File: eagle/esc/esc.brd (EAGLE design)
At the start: 101.6 x 50.8 mm, 88 parts, among them IC1 DRV8305NPHPR, IC2 STM32L431CCT6LQFP48, IC3 FT232RL, J2 ARM10-CON, T1 CSD17573Q5B, T2 CSD17573Q5B, T3 CSD17573Q5B, T4 CSD17573Q5B, T5 CSD17573Q5B, T6 CSD17573Q5B, U1 LD1117S50TR1, U2 MIC5319-3.3YD5-TR, X1 C-GRID-02-15-19, X2 MINI-USB-32005-301

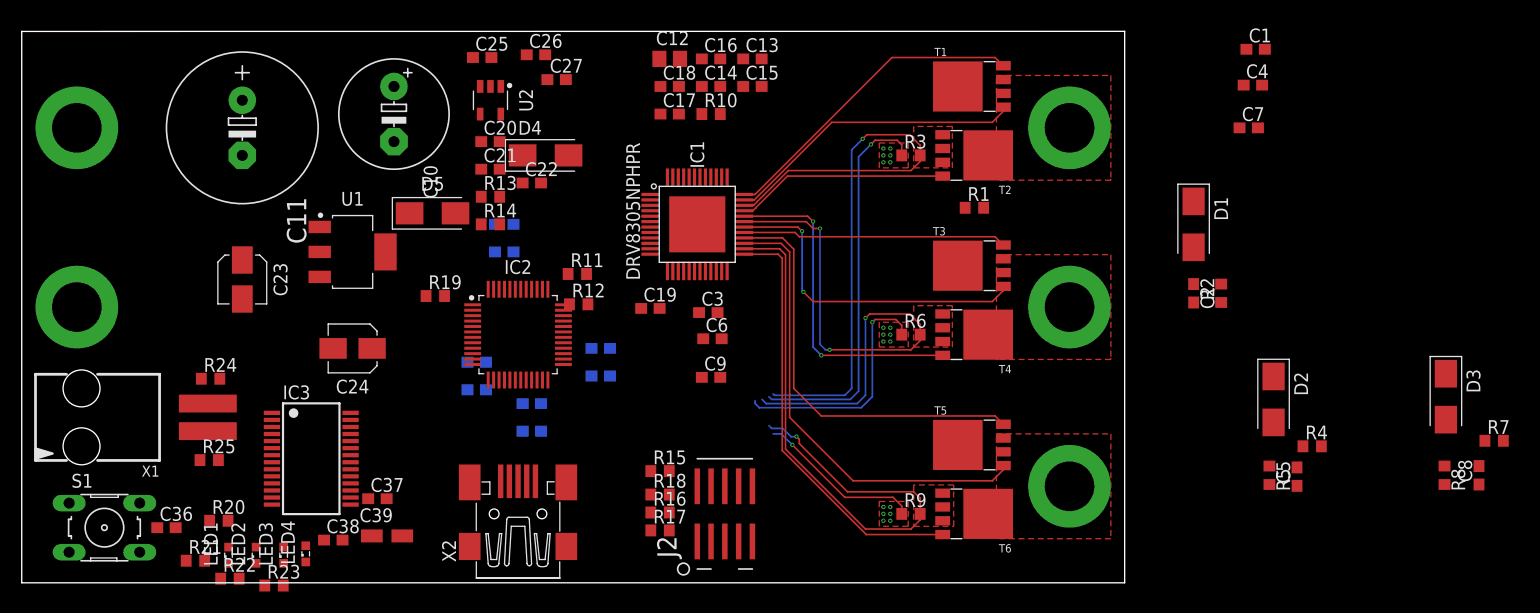
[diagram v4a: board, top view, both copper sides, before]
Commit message: updated pin mappings - changed a bunch for better placements
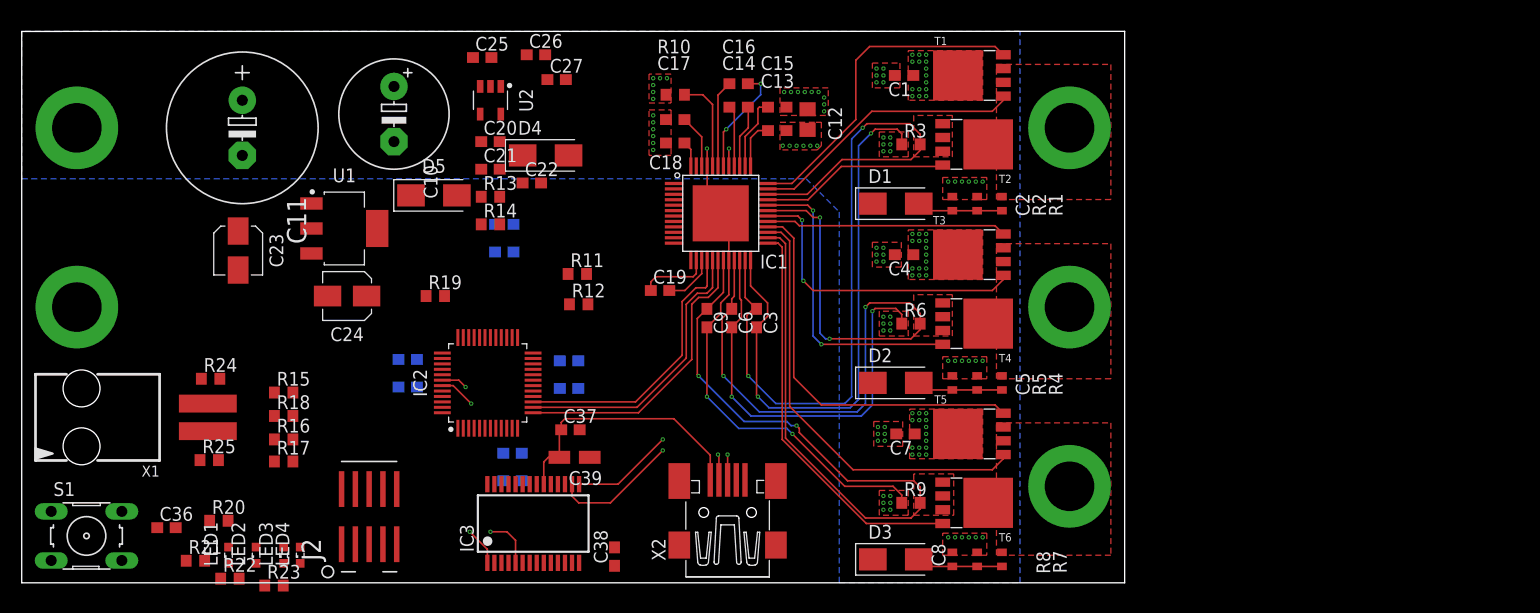
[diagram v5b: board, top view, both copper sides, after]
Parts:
- C2, C5, C8: device resistor:C0603 -> resistor:C0402
- R1, R2, R4, R5, R7, R8: device resistor:R0603 -> resistor:R0402
- moved D3 52.8 mm to (80.5, 2.16), turned to 0 degrees
- moved C8 49.1 mm to (85.7, 2.16)
- moved R7 46.6 mm to (90.3, 2.16), turned to 90 degrees
- moved R8 43.7 mm to (88.0, 2.16)
- moved C7 42.4 mm to (81.4, 13.7), turned to 180 degrees
- moved C4 35.7 mm to (81.3, 30.2), turned to 180 degrees
- moved R15 35.4 mm to (24.1, 17.5)
- moved R18 35.4 mm to (24.1, 15.4)
- moved R16 35.3 mm to (24.1, 13.2)
- moved R17 35.2 mm to (24.1, 11.2)
- moved D2 34.8 mm to (80.5, 18.4), turned to 0 degrees
- moved C5 32.9 mm to (85.7, 18.4)
- moved J2 32.8 mm to (32.0, 6.10)
- moved C1 32.5 mm to (81.3, 46.7), turned to 180 degrees
- moved R4 29.2 mm to (90.3, 18.4), turned to 90 degrees
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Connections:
- net ASENSE: now also IC2.19; no longer IC2.17
- net CSENSE: now also IC2.17; no longer IC2.19
- net SO1: now also IC2.15; no longer IC2.13
- net SO3: now also IC2.13; no longer IC2.15
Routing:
- net GND: track 73.7 -> 146.0 mm, vias 22 -> 74
- net SO3: track 0.00 -> 27.3 mm
- net SO2: track 0.00 -> 26.5 mm
- net SO1: track 0.00 -> 25.8 mm
- net N$15: track 0.00 -> 24.5 mm
- net UART_RX: track 0.00 -> 20.6 mm, vias 0 -> 2
- net N$20: track 0.00 -> 19.5 mm, vias 0 -> 2
- net UART_TX: track 0.00 -> 19.4 mm, vias 0 -> 2
- net N$21: track 0.00 -> 19.4 mm, vias 0 -> 2
- net SL_C: track 56.7 -> 74.2 mm, vias 1 -> 2
- net SL_B: track 51.9 -> 67.8 mm, vias 3 -> 4
- net SL_A: track 56.2 -> 70.8 mm, vias 1 -> 2
- net N$2: track 0.00 -> 10.2 mm, vias 0 -> 2
- net N$8: track 0.00 -> 8.69 mm
- net N$6: track 0.00 -> 8.07 mm
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- added copper zone on layer 1, net VDD
- added copper zone on layer 16, net VDD
